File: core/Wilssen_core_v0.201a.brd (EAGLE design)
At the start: 25.4 x 64.8 mm, 28 parts, among them Q1 8Mhz, U1 MAX1555, U2 3.3V, U3 ATMEGA168/ATMEGA328, X1 USBSMD

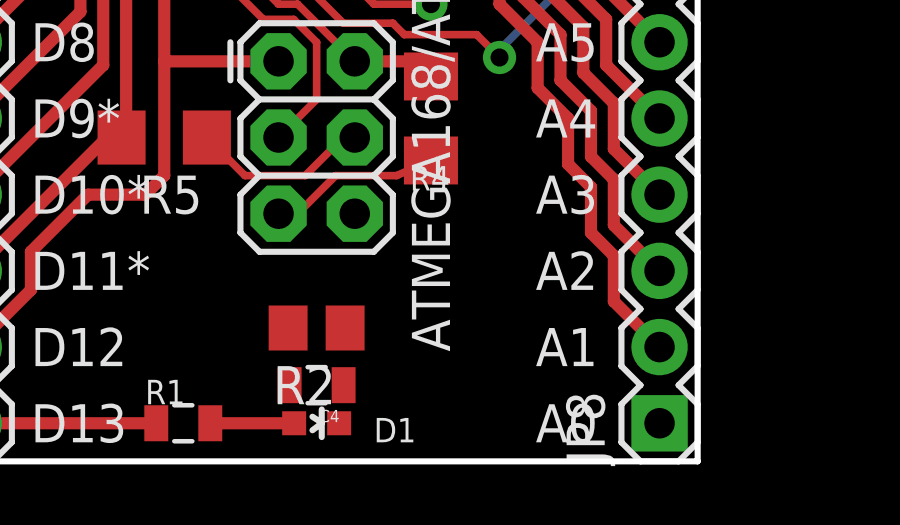
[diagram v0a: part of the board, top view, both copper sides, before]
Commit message: added external voltage reference
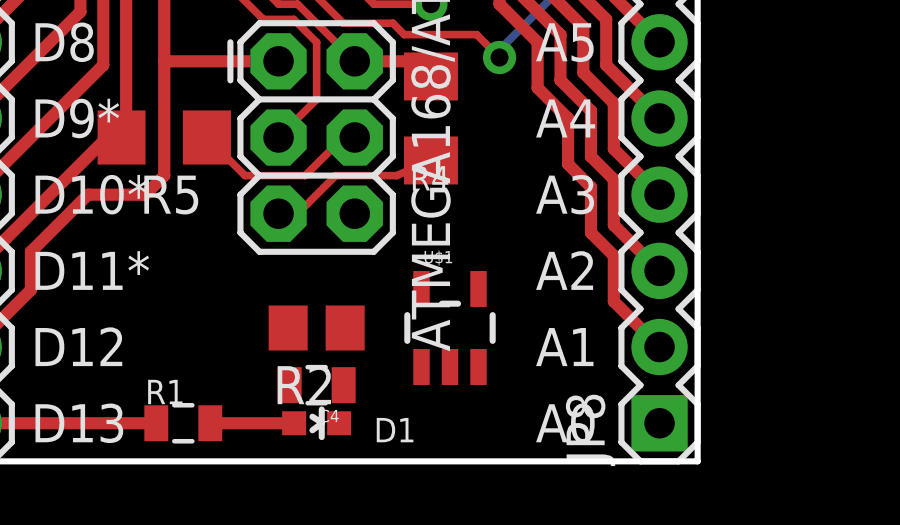
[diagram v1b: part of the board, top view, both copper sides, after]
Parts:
- added U$1: LM4128-2.5VREF, SparkFun-PowerIC:SOT23-5
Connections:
- new net N$3: U$1.5, U3.20
- net GND: now also U$1.2
- net VCC: now also U$1.3, U$1.4
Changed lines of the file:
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@@
 <layer number="17" name="Pads" color="2" fill="1" visible="yes" active="yes"/>
 <layer number="18" name="Vias" color="2" fill="1" visible="yes" active="yes"/>
-<layer number="19" name="Unrouted" color="6" fill="1" visible="no" active="yes"/>
+<layer number="19" name="Unrouted" color="6" fill="1" visible="yes" active="yes"/>
 <layer number="20" name="Dimension" color="6" fill="1" visible="yes" active="yes"/>
 <layer number="21" name="tPlace" color="16" fill="1" visible="yes" active="yes"/>
@@
 <element name="JP9" library="SparkFun-Connectors" package="1X06" value="" x="24.13" y="21.59" rot="R90"/>
 <element name="R5" library="rcl" package="R1206" value="3R3" x="7.62" y="10.795" rot="R180"/>
+<element name="U$1" library="SparkFun-PowerIC" package="SOT23-5" value="LM4128-2.5VREF" x="17.145" y="4.445"/>
 </elements>
 <signals>
@@
 <contactref element="C6" pad="1"/>
 <contactref element="JP9" pad="1"/>
+<contactref element="U$1" pad="2"/>
 <wire x1="17.1751" y1="49.53" x2="46.498" y2="59.165" width="0" layer="19" extent="1-1"/>
 <wire x1="14.605" y1="53.34" x2="17.1751" y2="49.53" width="0" layer="19" extent="1-1"/>
@@
 <wire x1="13.35" y1="44.45" x2="12.05" y2="45.72" width="0" layer="19" extent="1-1"/>
 <wire x1="12.7" y1="32.89" x2="13.35" y2="44.45" width="0" layer="19" extent="1-1"/>
-<wire x1="12.7" y1="28.713" x2="12.7" y2="32.89" width="0" layer="19" extent="1-1"/>
-<wire x1="12.29" y1="25.2576" x2="12.7" y2="28.713" width="0" layer="19" extent="1-1"/>
-<wire x1="13.89" y1="25.2576" x2="12.29" y2="25.2576" width="0" layer="19" extent="1-1"/>
+<wire x1="12.29" y1="25.2576" x2="13.89" y2="25.2576" width="0" layer="19" extent="1-1"/>
 <wire x1="12.45" y1="23.305" x2="12.29" y2="25.2576" width="0" layer="19" extent="1-1"/>
 <wire x1="13.45" y1="23.305" x2="12.45" y2="23.305" width="0" layer="19" extent="1-1"/>
 <wire x1="12.95" y1="18.605" x2="12.45" y2="23.305" width="0" layer="19" extent="1-1"/>
 <wire x1="13.09" y1="16.6724" x2="12.95" y2="18.605" width="0" layer="19" extent="1-1"/>
-<wire x1="5.715" y1="33.285" x2="12.7" y2="32.89" width="0" layer="19" extent="1-1"/>
-<wire x1="1.27" y1="31.75" x2="5.715" y2="33.285" width="0" layer="19" extent="1-1"/>
-<wire x1="19.685" y1="31.485" x2="12.7" y2="32.89" width="0" layer="19" extent="1-1"/>
-<wire x1="13.97" y1="8.255" x2="13.09" y2="16.6724" width="0" layer="19" extent="1-1"/>
-<wire x1="13.65" y1="4.445" x2="13.97" y2="8.255" width="0" layer="19" extent="1-1"/>
-<wire x1="13.6" y1="2.54" x2="13.65" y2="4.445" width="0" layer="19" extent="1-1"/>
-<wire x1="13.45" y1="1.27" x2="13.6" y2="2.54" width="0" layer="19" extent="1-1"/>
-<wire x1="24.13" y1="21.59" x2="13.45" y2="23.305" width="0" layer="19" extent="1-1"/>
 </signal>
 <signal name="VCC" class="1">
@@
 <wire x1="16.005" y1="13.335" x2="16.51" y2="12.83" width="0.4064" layer="1"/>
 <contactref element="ATMEGA168/ATMEGA328" pad="20"/>
+<contactref element="U$1" pad="4"/>
+<contactref element="U$1" pad="3"/>
 <wire x1="12.7" y1="35.69" x2="14.5749" y2="48.58" width="0" layer="19" extent="1-1"/>
 <wire x1="12.7" y1="26.913" x2="12.7" y2="35.69" width="0" layer="19" extent="1-1"/>
 <wire x1="12.45" y1="18.605" x2="11.45" y2="18.605" width="0" layer="19" extent="1-1"/>
+<wire x1="18.095" y1="5.7451" x2="16.51" y2="12.83" width="0" layer="19" extent="1-1"/>
+<wire x1="18.095" y1="3.1449" x2="18.095" y2="5.7451" width="0" layer="19" extent="1-1"/>
 <wire x1="24.13" y1="26.67" x2="13.09" y2="26.523" width="0" layer="19" extent="1-1"/>
 <wire x1="1.27" y1="34.29" x2="12.7" y2="35.69" width="0" layer="19" extent="1-1"/>
@@
 <signal name="XTAL2">
 <contactref element="U3" pad="8"/>
-<wire x1="9.89" y1="25.2576" x2="9.3499" y2="25.2576" width="0" layer="19" extent="1-16"/>
-<wire x1="9.3499" y1="25.2576" x2="8.325" y2="26.2825" width="0" layer="19" extent="1-16"/>
 <contactref element="ATMEGA168/ATMEGA328" pad="8"/>
 <wire x1="10.95" y1="23.305" x2="9.89" y2="24.365" width="0.254" layer="1"/>
@@
 <contactref element="C6" pad="2"/>
 <wire x1="5.715" y1="31.485" x2="7.874" y2="29.845" width="0" layer="19" extent="1-1"/>
-<wire x1="8.325" y1="26.2825" x2="7.874" y2="29.845" width="0" layer="19" extent="1-1"/>
+<wire x1="9.89" y1="25.2576" x2="7.874" y2="29.845" width="0" layer="19" extent="1-1"/>
 </signal>
 <signal name="N$2">
@@
 <wire x1="17.1751" y1="50.48" x2="17.145" y2="53.34" width="0" layer="19" extent="1-1"/>
 <wire x1="17.1751" y1="48.58" x2="17.1751" y2="50.48" width="0" layer="19" extent="1-1"/>
-<wire x1="12.05" y1="44.45" x2="17.1751" y2="48.58" width="0" layer="19" extent="1-1"/>
+<wire x1="10.8251" y1="50.48" x2="17.1751" y2="50.48" width="0" layer="19" extent="1-1"/>
+<wire x1="12.05" y1="44.45" x2="10.8251" y2="50.48" width="0" layer="19" extent="1-1"/>
 <wire x1="13.45" y1="41.275" x2="12.05" y2="44.45" width="0" layer="19" extent="1-1"/>
 <wire x1="13.65" y1="38.735" x2="13.45" y2="41.275" width="0" layer="19" extent="1-1"/>
-<wire x1="10.8251" y1="50.48" x2="12.05" y2="44.45" width="0" layer="19" extent="1-1"/>
 </signal>
 <signal name="N$8">
@@
 <contactref element="ATMEGA168/ATMEGA328" pad="29"/>
 </signal>
+<signal name="N$3">
+<contactref element="U$1" pad="5"/>
+<contactref element="U3" pad="20"/>
+<wire x1="16.195" y1="5.7451" x2="12.29" y2="16.6724" width="0" layer="19" extent="1-1"/>
+</signal>
 </signals>
